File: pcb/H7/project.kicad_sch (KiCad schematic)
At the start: 61 parts, among them J3 bt, J4 rst, U11 STM32H723VGT6, U14 TPS5430DDAR, U17 LDL1117S33R, U23 W25Q128FVSIG

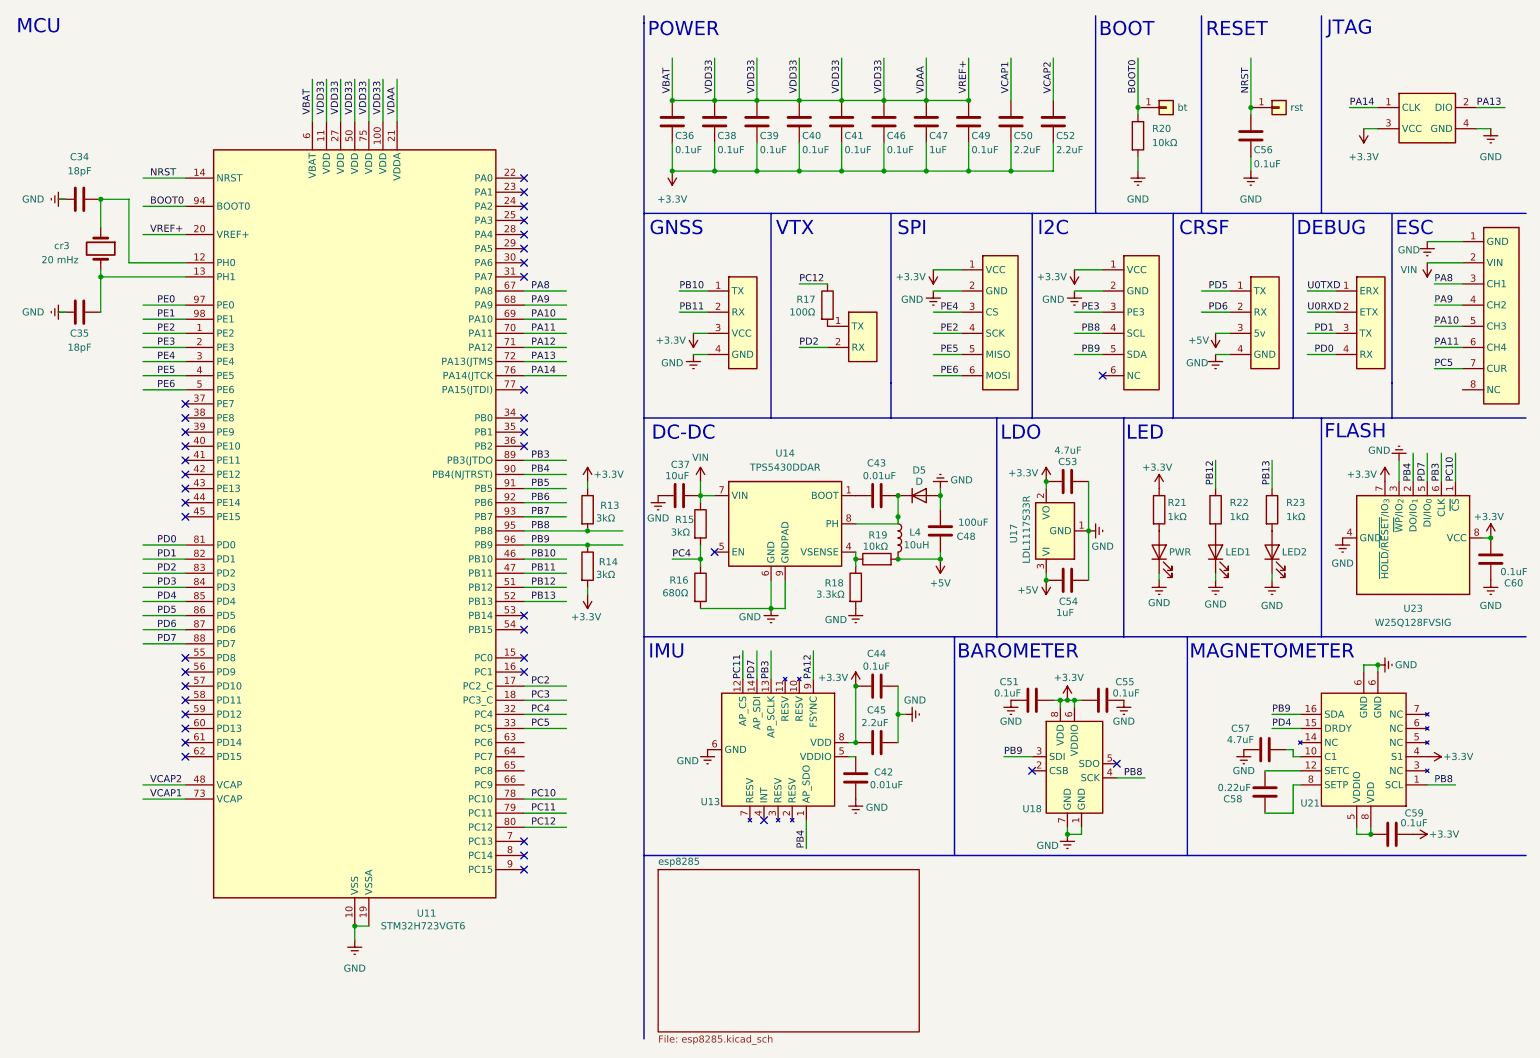
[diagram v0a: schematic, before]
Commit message: schematic source updated
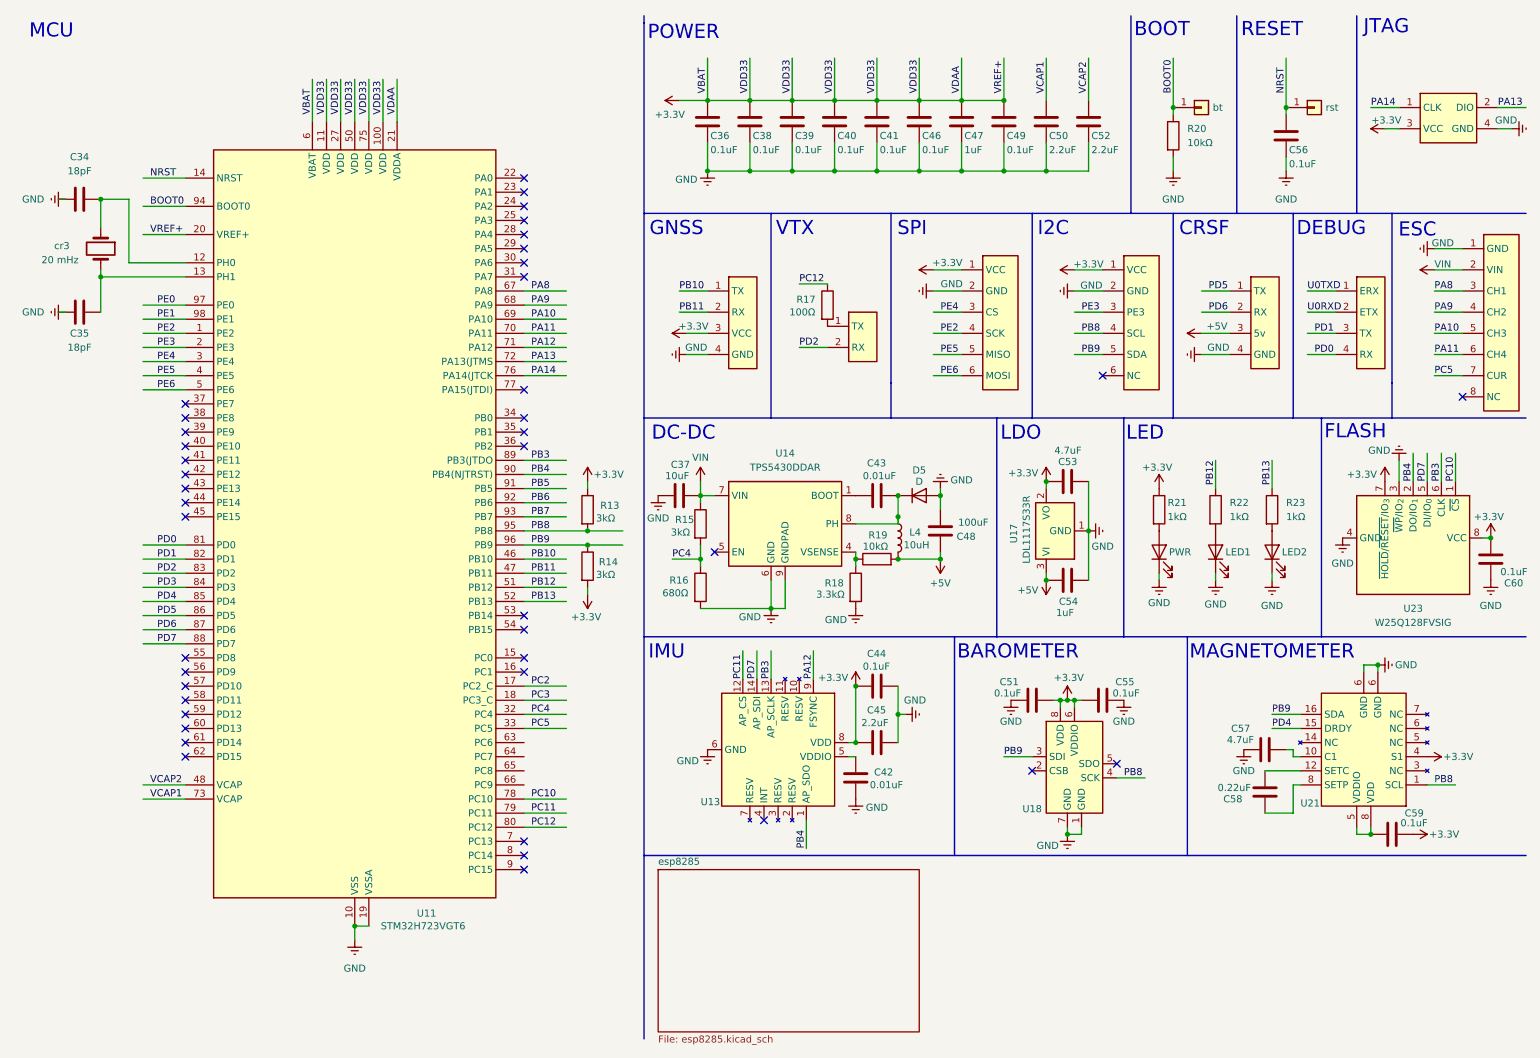
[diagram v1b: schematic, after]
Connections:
- net VBAT is gone; now on net +3.3V: C36.1, C38.1, C39.1, C40.1, C41.1, C46.1, C47.1, C49.1, U11.100 (VDD), U11.11 (VDD), U11.20 (VREF+), U11.21 (VDDA), U11.27 (VDD), U11.50 (VDD), U11.6 (VBAT), U11.75 (VDD)
- net +3.3V: no longer C36.2, C38.2, C39.2, C40.2, C41.2, C46.2, C47.2, C49.2, C50.2, C52.2
- net GND: now also C36.2, C38.2, C39.2, C40.2, C41.2, C46.2, C47.2, C49.2, C50.2, C52.2
- new net: C59.2, U21.5 (VDDIO), U21.8 (SETP)
- now unconnected: U21.5 (VDDIO)
- no-connect marks 41 -> 42
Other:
- moved on the sheet: C36, C38, C39, C40, C41, C46, C47, C49, C50, C52, C56, R20

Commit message: trying to fix dshot issue with high frequency timer, schematic numbers fix
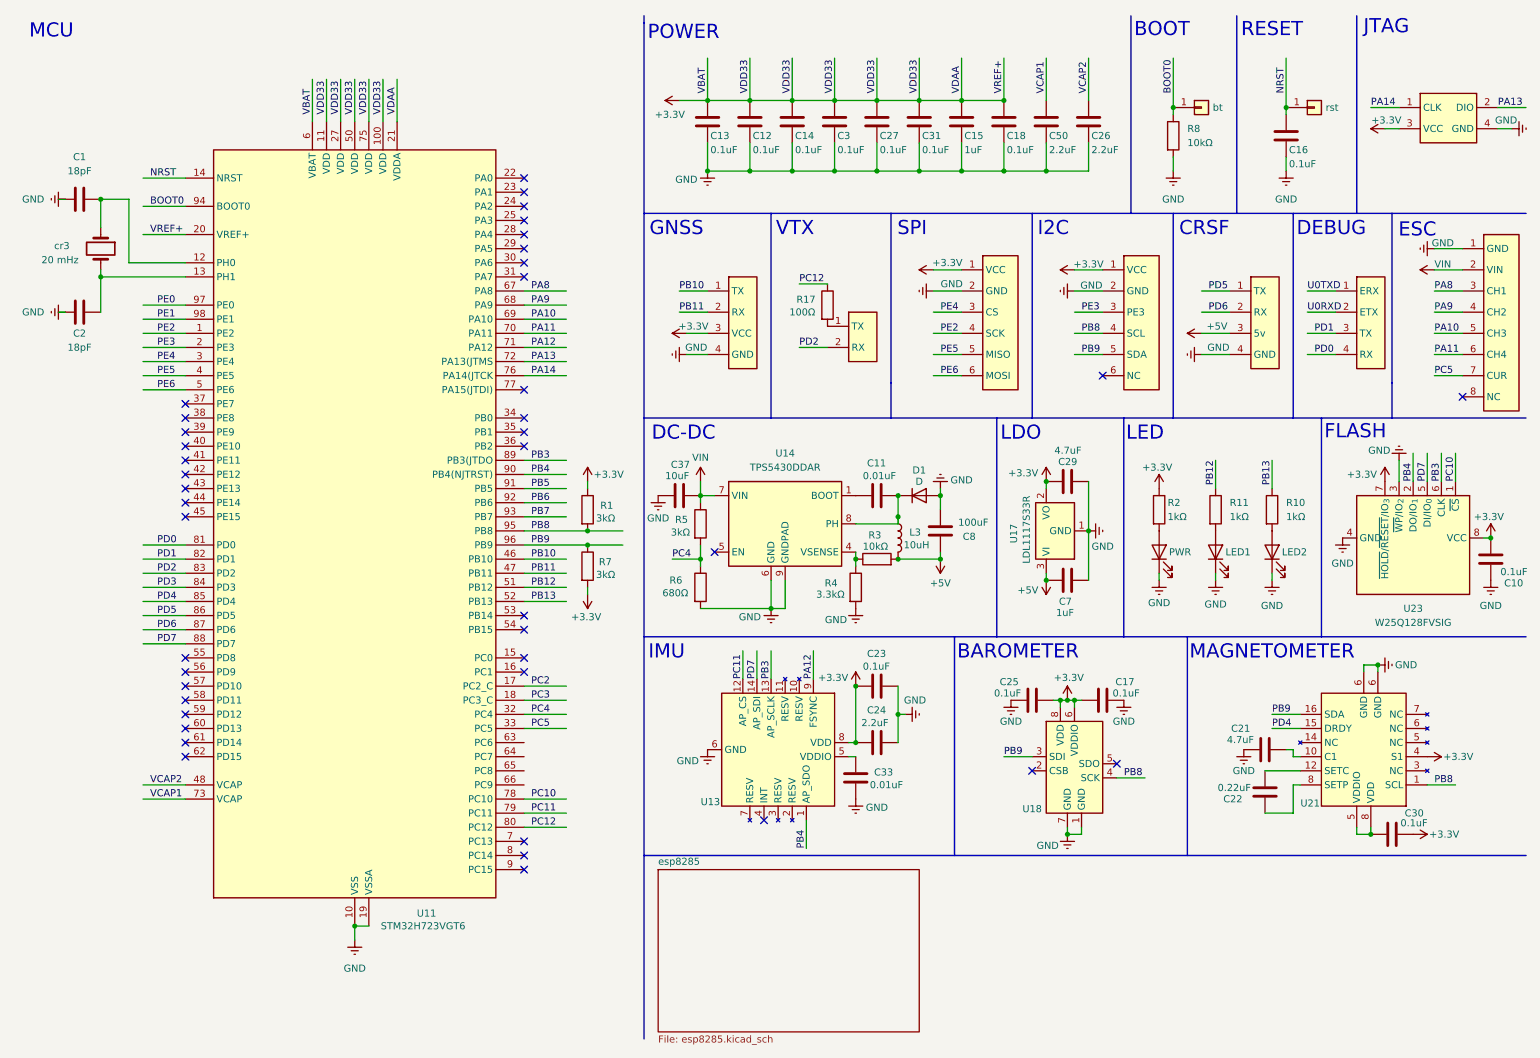
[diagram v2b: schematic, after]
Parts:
- renumbered C34 to C1, C60 to C10, C43 to C11, C38 to C12, C36 to C13, C39 to C14, C47 to C15, C56 to C16, C55 to C17, C49 to C18, C35 to C2, C57 to C21, C58 to C22, C44 to C23, C45 to C24, C51 to C25, C52 to C26, C41 to C27, C53 to C29, C40 to C3, C59 to C30, C46 to C31, C42 to C33, C54 to C7, C48 to C8, D5 to D1, L4 to L3, R13 to R1, R23 to R10, R22 to R11, R21 to R2, R19 to R3, R18 to R4, R15 to R5, R16 to R6, R14 to R7, R20 to R8
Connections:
- new net: C30.2, U21.5 (VDDIO), U21.8 (SETP)
- now unconnected: U21.5 (VDDIO)

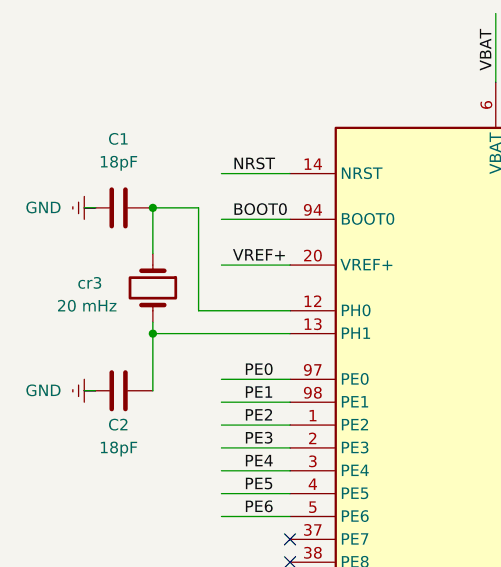
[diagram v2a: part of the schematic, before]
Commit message: esp8266 spi fix
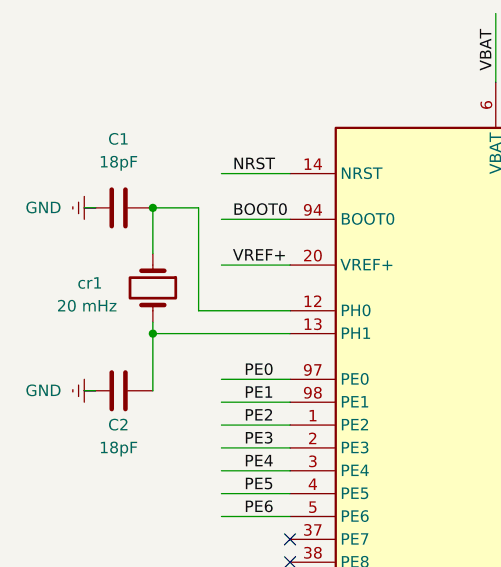
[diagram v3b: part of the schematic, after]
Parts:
- renumbered cr3 to cr1
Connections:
- new net: C30.2, U21.5 (VDDIO), U21.8 (SETP)
- now unconnected: U21.5 (VDDIO)
